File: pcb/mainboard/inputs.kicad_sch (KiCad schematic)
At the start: 106 parts, among them U10 MAX40026, U11 MAX40026, U12 MAX40026, U13 MAX40026, U14 MAX40026, U15 MAX40026, U16 MAX40026, U17 MAX40026, U18 MAX40026, U19 MAX40026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

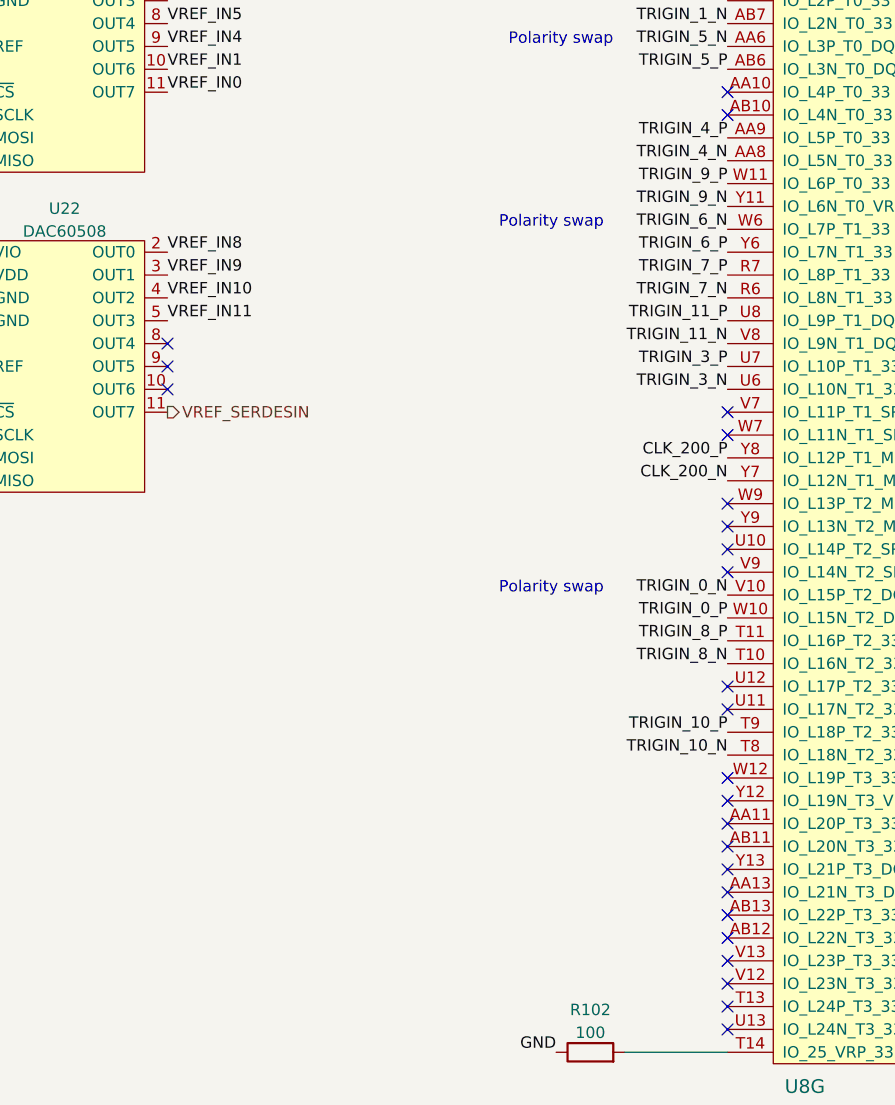
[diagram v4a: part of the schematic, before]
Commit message: Continued layout, started plane fills. Everything routed except 1V8 regulator
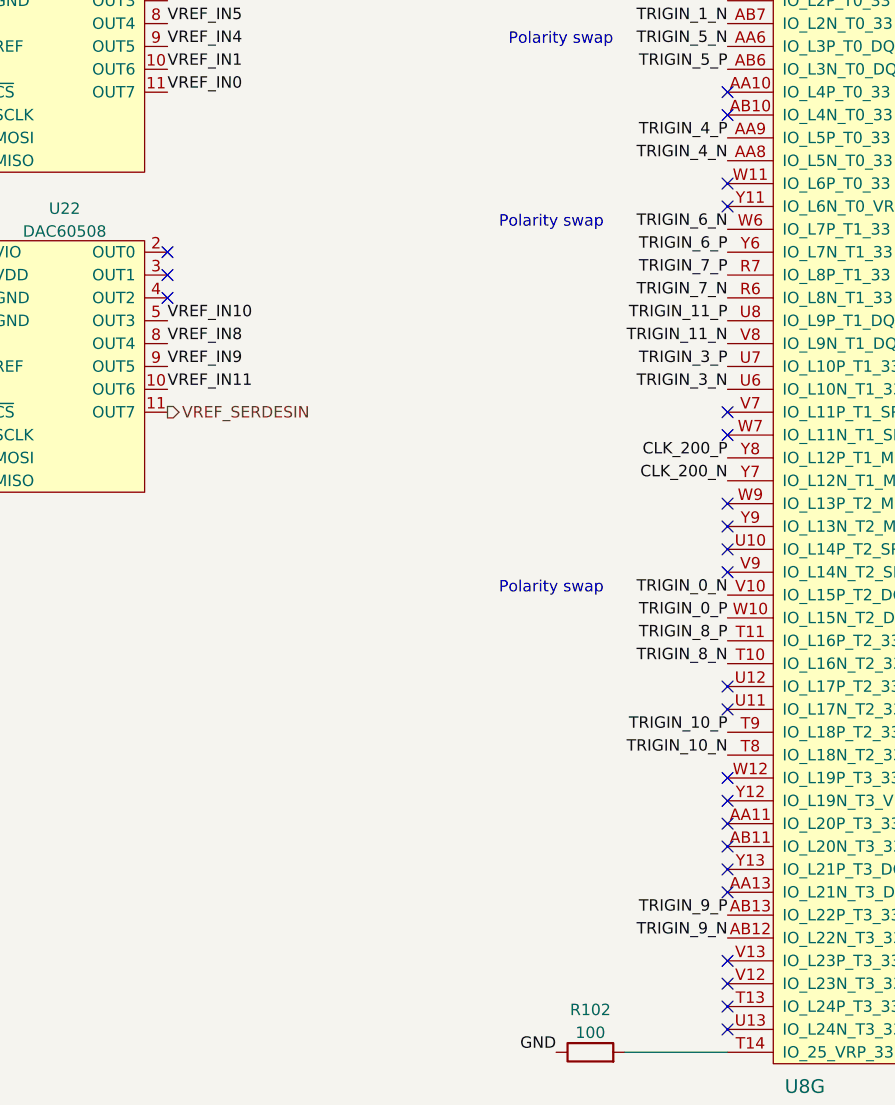
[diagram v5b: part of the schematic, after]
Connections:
- net TRIGIN_9_N: now also U8.AB12 (IO_L22N_T3_33); no longer U8.Y11 (IO_L6N_T0_VREF_33)
- net TRIGIN_9_P: now also U8.AB13 (IO_L22P_T3_33); no longer U8.W11 (IO_L6P_T0_33)
- net VREF_IN10: now also U22.5 (OUT3); no longer U22.4 (OUT2)
- net VREF_IN11: now also U22.10 (OUT6); no longer U22.5 (OUT3)
- net VREF_IN8: now also U22.8 (OUT4); no longer U22.2 (OUT0)
- net VREF_IN9: now also U22.9 (OUT5); no longer U22.3 (OUT1)
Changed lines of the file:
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@@
   (title_block
     (title "Trigger Crossbar")
-    (date "2023-12-22")
+    (date "2023-12-25")
     (rev "0.1")
     (company "Antikernel Labs")
@@
   )
   (no_connect (at 271.78 124.46))
-  (no_connect (at 271.78 139.7))
+  (no_connect (at 271.78 58.42))
   (no_connect (at 271.78 134.62))
+  (no_connect (at 209.55 68.58))
   (no_connect (at 271.78 83.82))
   (no_connect (at 271.78 93.98))
   (no_connect (at 271.78 111.76))
+  (no_connect (at 271.78 55.88))
   (no_connect (at 271.78 144.78))
   (no_connect (at 271.78 45.72))
@@
   (no_connect (at 271.78 149.86))
   (no_connect (at 271.78 127))
-  (no_connect (at 209.55 73.66))
   (no_connect (at 271.78 114.3))
   (no_connect (at 271.78 147.32))
+  (no_connect (at 209.55 63.5))
   (no_connect (at 271.78 99.06))
-  (no_connect (at 209.55 76.2))
-  (no_connect (at 271.78 137.16))
-  (no_connect (at 209.55 78.74))
+  (no_connect (at 209.55 66.04))
   (no_connect (at 271.78 121.92))
   (no_connect (at 271.78 81.28))
@@
     (effects (font (size 1.27 1.27)) (justify right bottom))
   )
-  (label "VREF_IN10" (at 209.55 68.58 0)
+  (label "VREF_IN10" (at 209.55 71.12 0)
     (effects (font (size 1.27 1.27)) (justify left bottom))
   )
@@
     (effects (font (size 1.27 1.27)) (justify right bottom))
   )
-  (label "VREF_IN11" (at 209.55 71.12 0)
+  (label "VREF_IN11" (at 209.55 78.74 0)
     (effects (font (size 1.27 1.27)) (justify left bottom))
   )
@@
     (effects (font (size 1.27 1.27)) (justify left bottom))
   )
-  (label "TRIGIN_9_P" (at 271.78 55.88 180)
+  (label "TRIGIN_9_P" (at 271.78 137.16 180)
     (effects (font (size 1.27 1.27)) (justify right bottom))
   )
@@
     (effects (font (size 1.27 1.27)) (justify right bottom))
   )
-  (label "VREF_IN8" (at 209.55 63.5 0)
+  (label "VREF_IN8" (at 209.55 73.66 0)
     (effects (font (size 1.27 1.27)) (justify left bottom))
   )
@@
     (effects (font (size 1.27 1.27)) (justify right bottom))
   )
-  (label "TRIGIN_9_N" (at 271.78 58.42 180)
+  (label "TRIGIN_9_N" (at 271.78 139.7 180)
     (effects (font (size 1.27 1.27)) (justify right bottom))
   )
@@
     (effects (font (size 1.27 1.27)) (justify right bottom))
   )
-  (label "VREF_IN9" (at 209.55 66.04 0)
-    (effects (font (size 1.27 1.27)) (justify left bottom))
-  )
+  (label "VREF_IN9" (at 209.55 76.2 0)
+    (effects (font (size 1.27 1.27)) (justify left bottom))
+  )
